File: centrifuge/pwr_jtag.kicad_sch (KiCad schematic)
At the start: 6 parts

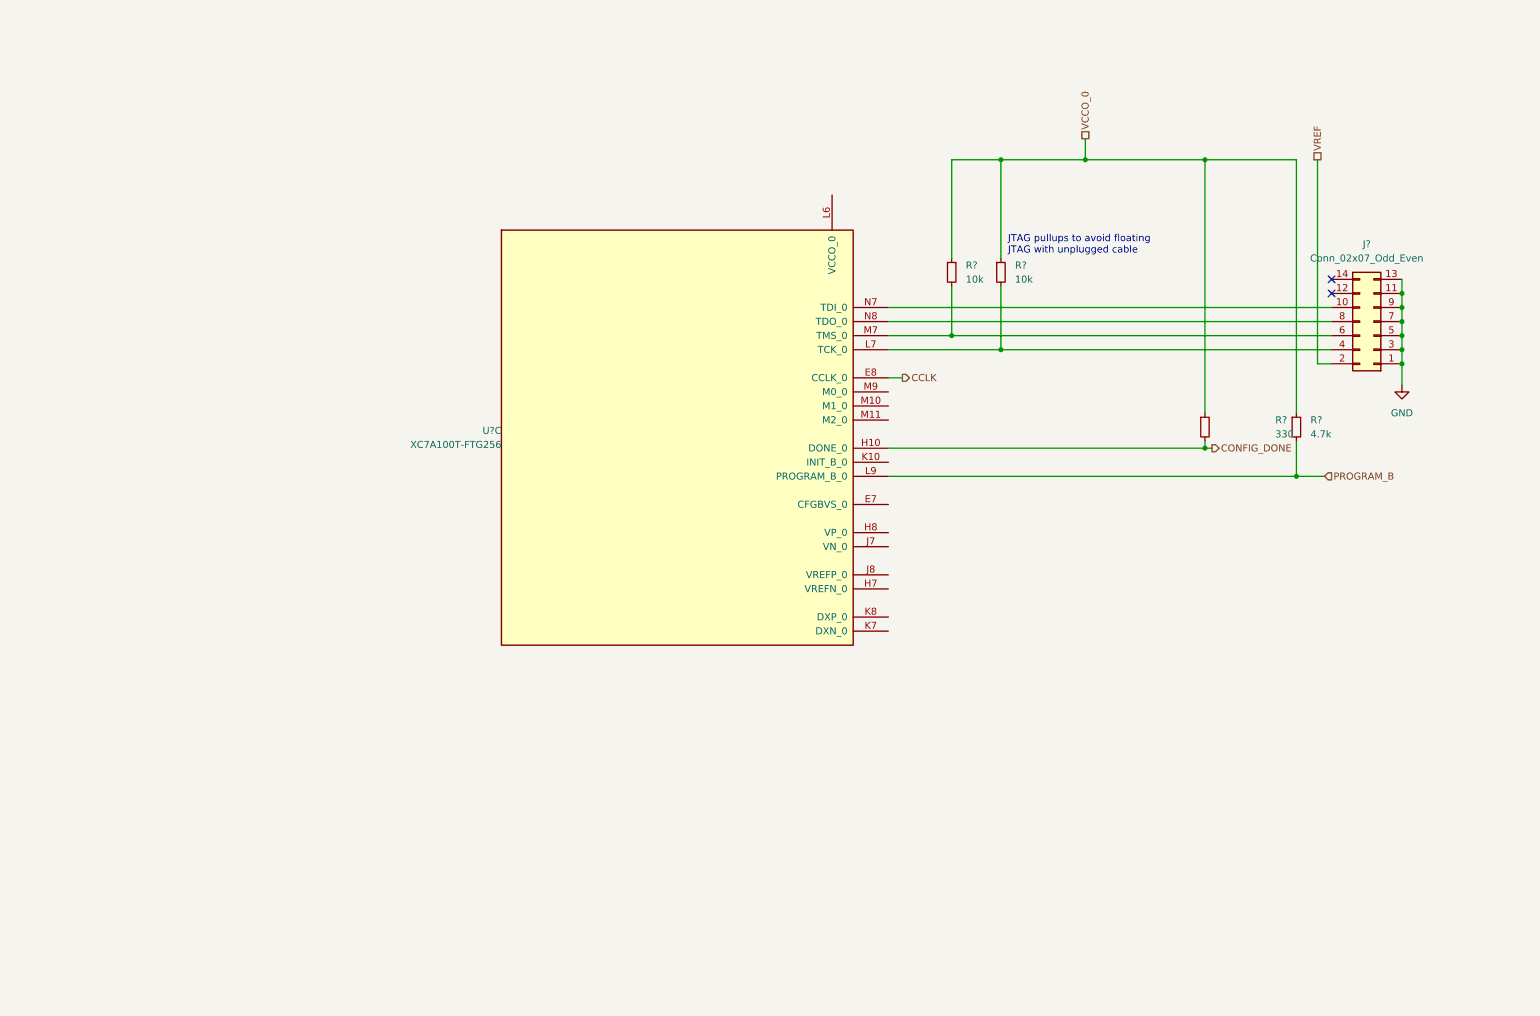
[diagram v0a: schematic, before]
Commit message: Made initial pin map of SRAM-FPGA and possible routing
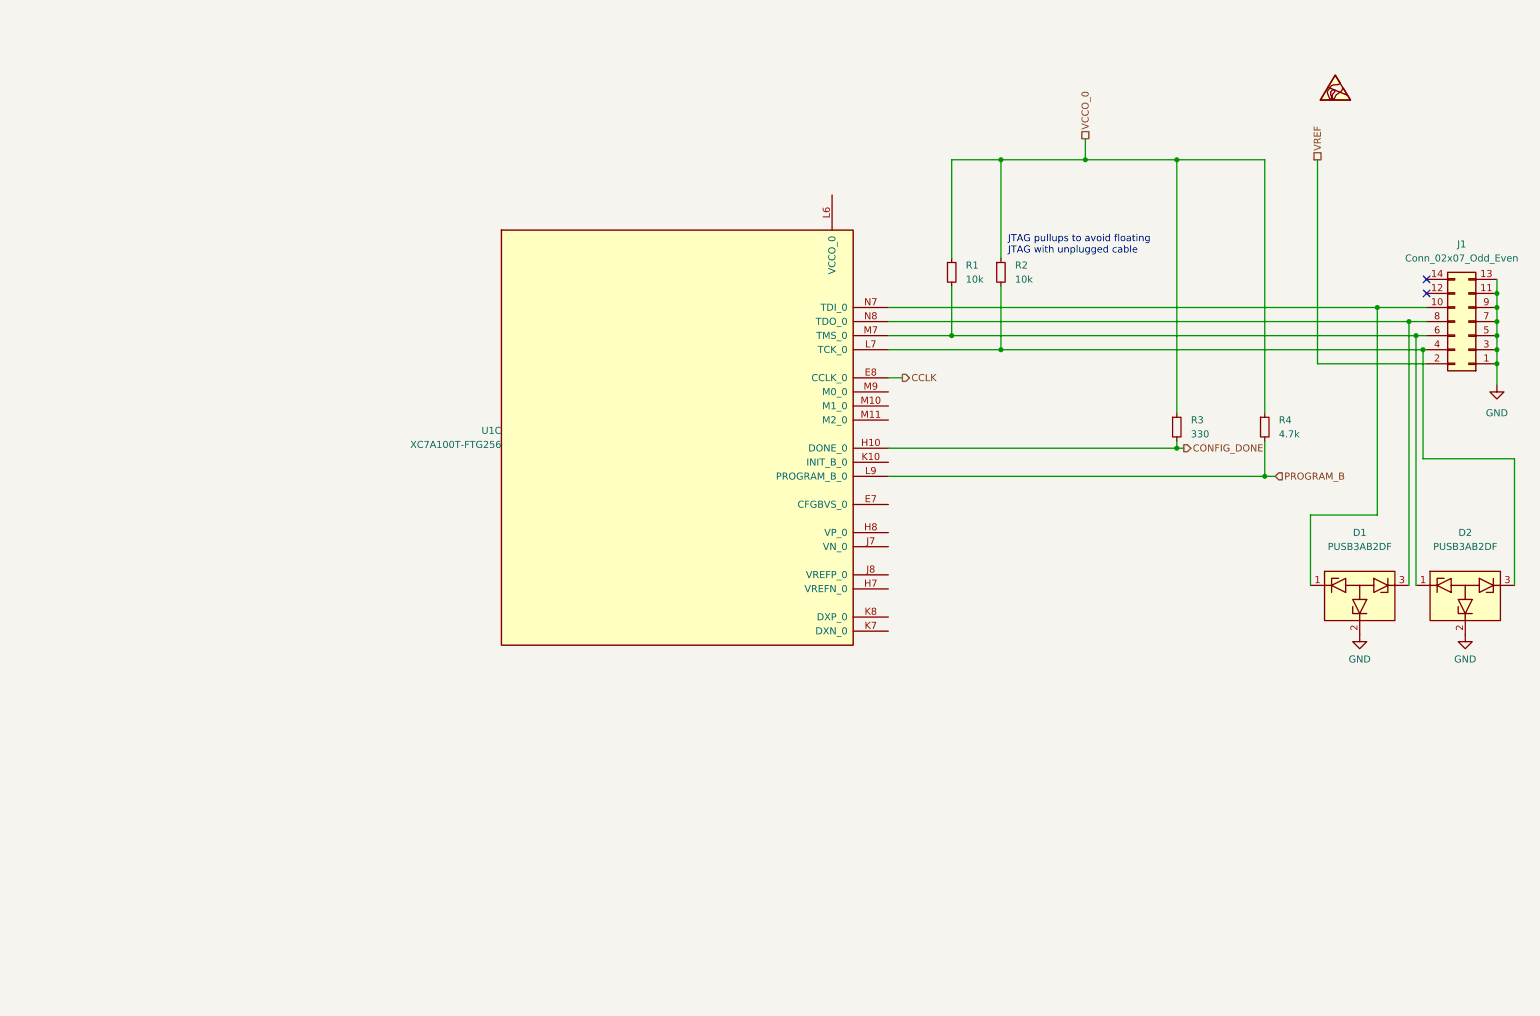
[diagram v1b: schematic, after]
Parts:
- added D1, D2: PUSB3AB2DF, symbol centrifuge_symbols:PUSB3AB2DF
- U1: renamed from U?; footprint (none) -> Package_BGA:Xilinx_FTG256
- gave numbers to parts that had none: 5
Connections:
- net GND: now also D1.2 (K2), D2.2 (K2)
- net at J1.4 (Pin_4), R2.2, U1.L7 (TCK_0): now also D2.3 (K3)
- net at J1.10 (Pin_10), U1.N7 (TDI_0): now also D1.1 (K1)
- net at J1.6 (Pin_6), R1.2, U1.M7 (TMS_0): now also D2.1 (K1)
- net at J1.8 (Pin_8), U1.N8 (TDO_0): now also D1.3 (K3)
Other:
- moved on the sheet: J1, R3, R4

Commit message: Completed majority of schematic, need to add decoupling but otherwise mostly ready
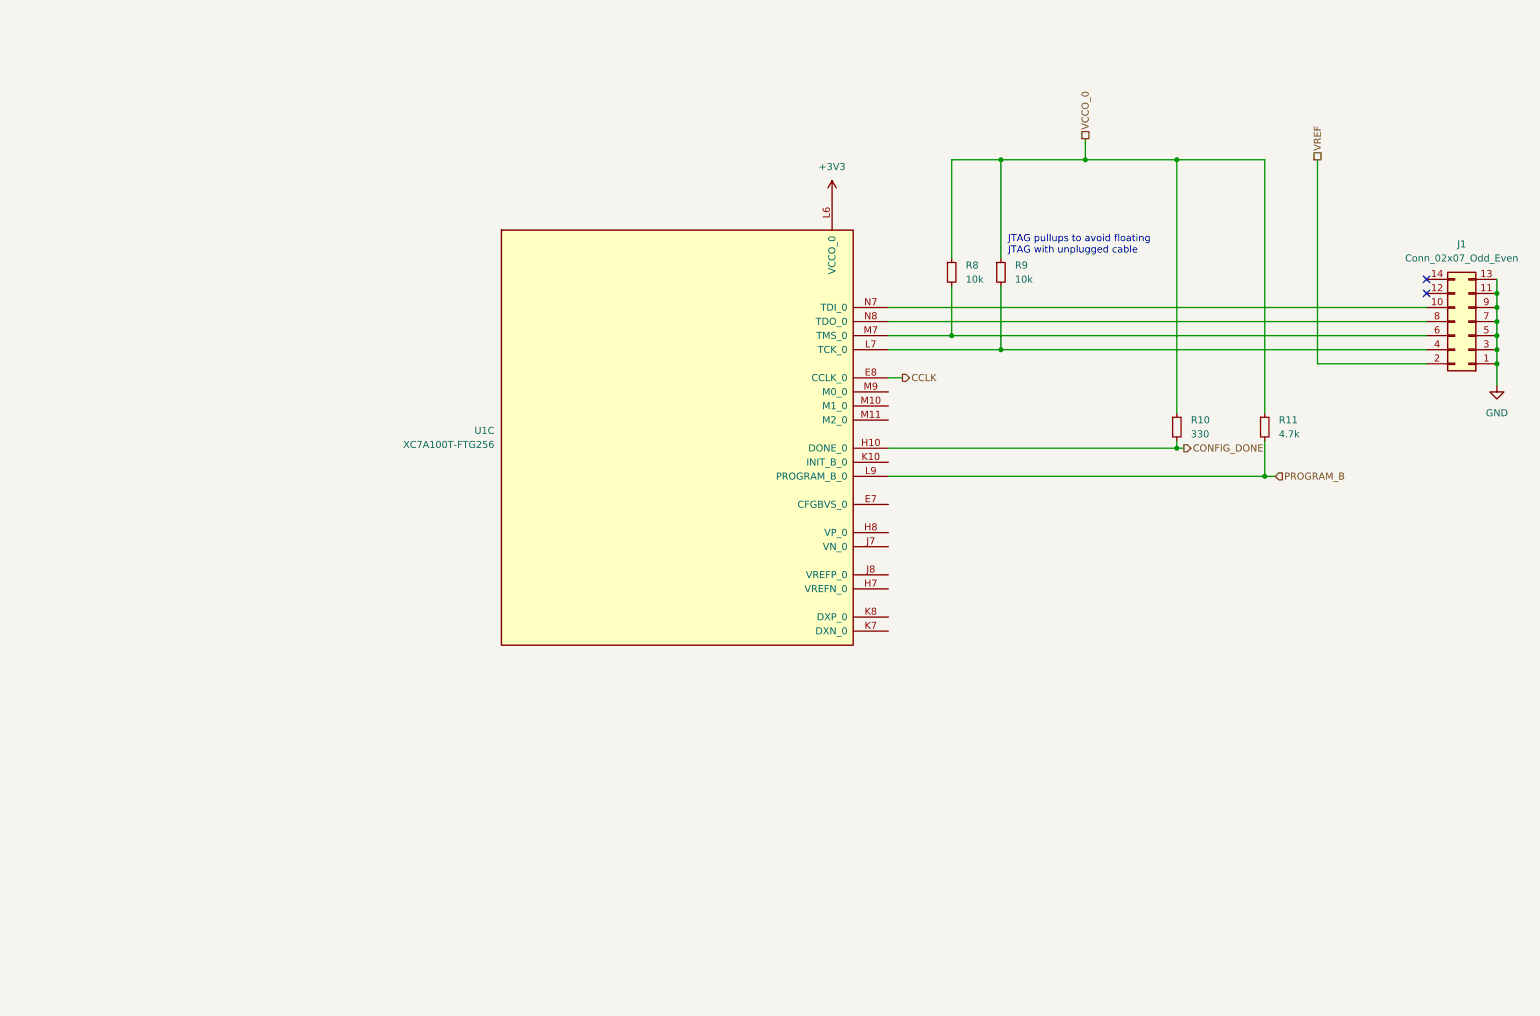
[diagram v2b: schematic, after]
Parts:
- removed D1, D2: PUSB3AB2DF, symbol centrifuge_symbols:PUSB3AB2DF
- J1: footprint (none) -> Connector_IDC:IDC-Header_2x07_P2.54mm_Vertical
- R10: renamed from R3; footprint (none) -> Resistor_SMD:R_0805_2012Metric_Pad1.20x1.40mm_HandSolder; Order Page (none) -> https://no.mouser.com/ProductDetail/Welwyn-Components-TT-El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
- R11: renamed from R4; footprint (none) -> Resistor_SMD:R_0805_2012Metric_Pad1.20x1.40mm_HandSolder; Order Page (none) -> https://no.mouser.com/ProductDetail/YAGEO/RC0805FR-074K7L?q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
- R8: renamed from R1; footprint (none) -> Resistor_SMD:R_0805_2012Metric_Pad1.20x1.40mm_HandSolder; Order Page (none) -> https://no.mouser.com/ProductDetail/YAGEO/RC0805FR-1310KL?q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
- R9: renamed from R2; footprint (none) -> Resistor_SMD:R_0805_2012Metric_Pad1.20x1.40mm_HandSolder; Order Page (none) -> https://no.mouser.com/ProductDetail/YAGEO/RC0805FR-1310KL?q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
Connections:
- net +3V3: now reaches U1.L6 (VCCO_0)
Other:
- title: VGA Centrifuge FPGA board -> VGA Centrifuge

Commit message: FPGA PCB design completed
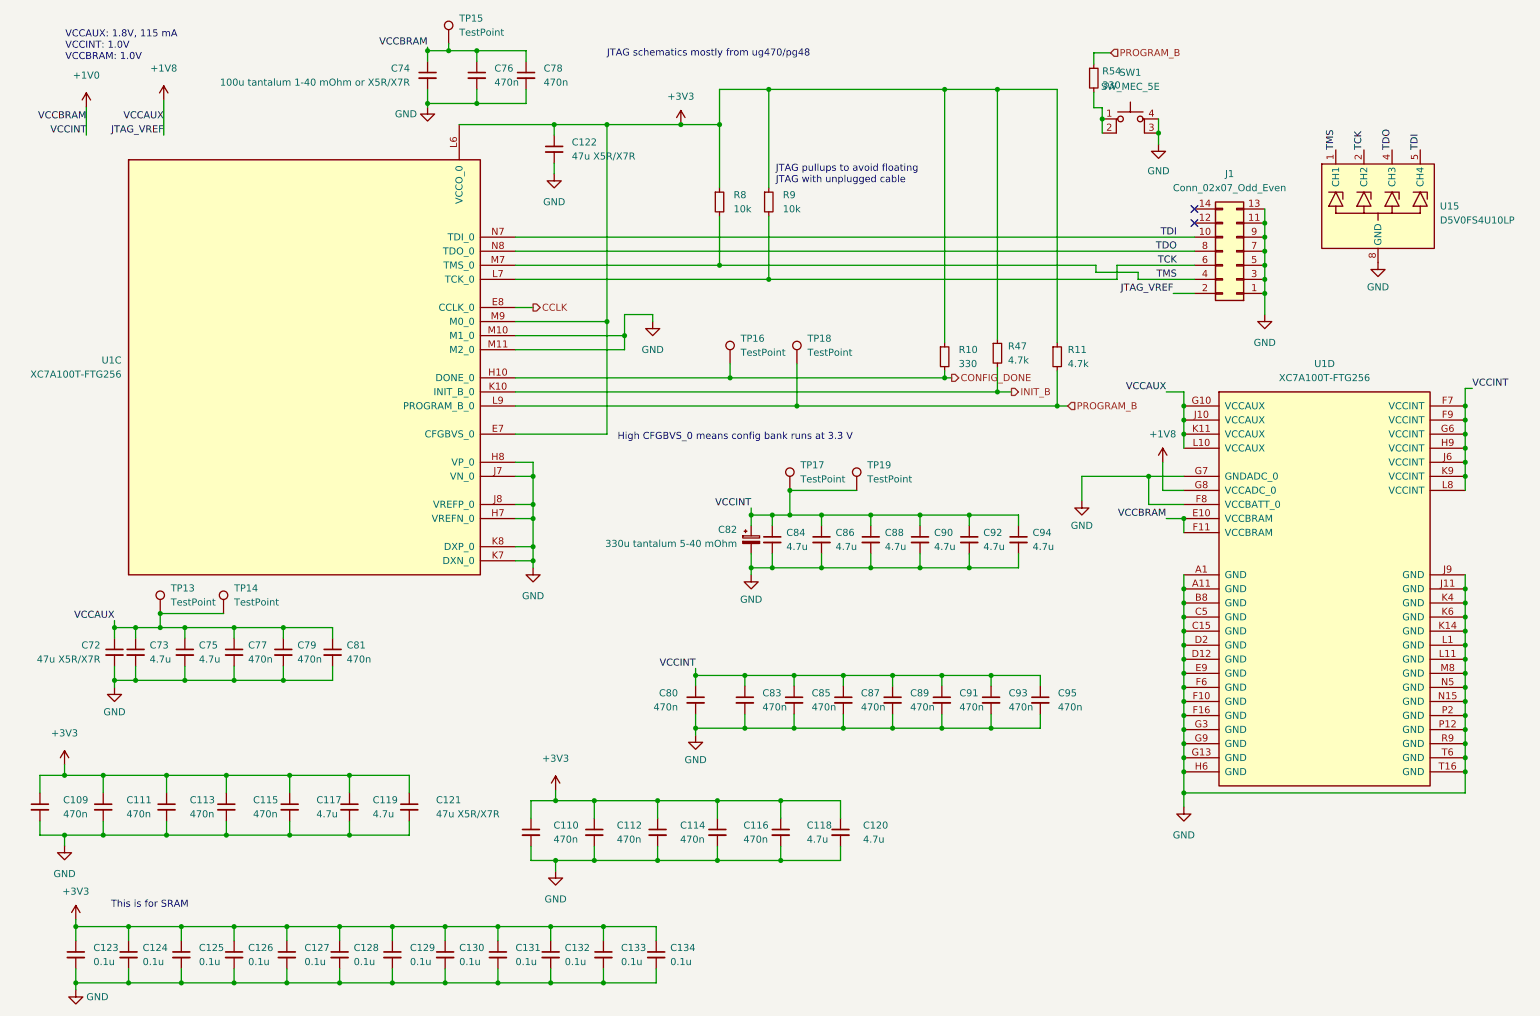
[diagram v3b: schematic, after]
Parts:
- added C109, C110, C111, C112, C113, C114, C115, C116, C76, C77, C78, C79, C80, C81, C83, C85, C87, C89, C91, C93, C95: 470n, Capacitor_SMD:C_0603_1608Metric_Pad1.08x0.95mm_HandSolder, symbol Device:C_Small
- added C117, C118, C119, C120, C73, C75, C84, C86, C88, C90, C92, C94: 4.7u, Capacitor_SMD:C_0805_2012Metric_Pad1.18x1.45mm_HandSolder, symbol Device:C_Small
- added C121, C122, C72: 47u X5R/X7R, Capacitor_SMD:C_1210_3225Metric_Pad1.33x2.70mm_HandSolder, symbol Device:C_Small
- added C123, C124, C125, C126, C127, C128, C129, C130, C131, C132, C133, C134: 0.1u, Capacitor_SMD:C_0805_2012Metric_Pad1.18x1.45mm_HandSolder, symbol Device:C_Small
- added C74: 100u tantalum 1-40 mOhm or X5R/X7R, Capacitor_SMD:C_1210_3225Metric_Pad1.33x2.70mm_HandSolder, symbol Device:C_Small
- added C82: 330u tantalum 5-40 mOhm, Capacitor_Tantalum_SMD:CP_EIA-7343-31_Kemet-D_Pad2.25x2.55mm_HandSolder, symbol Device:C_Polarized_Small
- added R47: 4.7k, Resistor_SMD:R_0805_2012Metric_Pad1.20x1.40mm_HandSolder, symbol Device:R_Small
- added R54: 330, Resistor_SMD:R_0805_2012Metric_Pad1.20x1.40mm_HandSolder, symbol Device:R_Small
- added SW1: SW_MEC_5E, centrifuge footprints:SW_Push_1P1T_NO_6x6mm_H9.5mm_modified, symbol Switch:SW_MEC_5E
- added TP13, TP14, TP15, TP16, TP17, TP18, TP19: TestPoint, TestPoint:TestPoint_Keystone_5015_Micro-Minature, symbol Connector:TestPoint
- added unit 4 of U1
- added U15: D5V0FS4U10LP, Package_DFN_QFN:Diodes_UDFN-10_1.0x2.5mm_P0.5mm, symbol centrifuge_symbols:D5V0FS4U10LP
- J1: footprint Connector_IDC:IDC-Header_2x07_P2.54mm_Vertical -> centrifuge footprints:878311411; Order Page (none) -> https://www.digikey.no/en/products/detail/molex/0878311411/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
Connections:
- net VCCO_0 is gone; now on net +3V3: R10.1, R11.1, R8.1, R9.1
- net +3V3: now also U1.E7 (CFGBVS_0), U1.M9 (M0_0), C109.1, C110.1, C111.1, C112.1, C113.1, C114.1, C115.1, C116.1, C117.1, C118.1, C119.1, C120.1, C121.1, C122.1, C123.1, C124.1, C125.1, C126.1, C127.1, C128.1, C129.1, C130.1, C131.1, C132.1, C133.1, C134.1, R47.1
- net CONFIG_DONE: now also TP16.1
- net GND: now also U1.H7 (VREFN_0), U1.H8 (VP_0), U1.J7 (VN_0), U1.J8 (VREFP_0), U1.K7 (DXN_0), U1.K8 (DXP_0), U1.M10 (M1_0), U1.M11 (M2_0), C109.2, C110.2, C111.2, C112.2, C113.2, C114.2, C115.2, C116.2, C117.2, C118.2, C119.2, C120.2, C121.2, C122.2, C123.2, C124.2, C125.2, C126.2, C127.2, C128.2, C129.2, C130.2, C131.2, C132.2, C133.2, C134.2, C72.2, C73.2, C74.2, C75.2, C76.2, C77.2, C78.2, C79.2, C80.2, C81.2, C82.2, C83.2, C84.2, C85.2, C86.2, C87.2, C88.2, C89.2, C90.2, C91.2, C92.2, C93.2, C94.2, C95.2, SW1.3 (K), SW1.4 (A), U1.A1 (GND), U1.A11 (GND), U1.B8 (GND), U1.C15 (GND), U1.C5 (GND), U1.D12 (GND), U1.D2 (GND), U1.E9 (GND), U1.F10 (GND), U1.F16 (GND), U1.F6 (GND), U1.F8 (VCCBATT_0), U1.G13 (GND), U1.G3 (GND), U1.G7 (GNDADC_0), U1.G9 (GND), U1.H6 (GND), U1.J11 (GND), U1.J9 (GND), U1.K14 (GND), U1.K4 (GND), U1.K6 (GND), U1.L1 (GND), U1.L11 (GND), U1.M8 (GND), U1.N15 (GND), U1.N5 (GND), U1.P12 (GND), U1.P2 (GND), U1.R9 (GND), U1.T16 (GND), U1.T6 (GND), U15.3 (GND), U15.8 (GND)
- net PROGRAM_B: now also R54.1, TP18.1
- net TCK: now reaches R9.2, U1.L7 (TCK_0)
- net TCK: now also J1.6 (Pin_6), U15.2 (CH2); no longer J1.4 (Pin_4)
- net TDI: now reaches J1.10 (Pin_10), U1.N7 (TDI_0)
- net TDI: now also U15.5 (CH4)
- net TMS: now reaches R8.2, U1.M7 (TMS_0)
- net TMS: now also J1.4 (Pin_4), U15.1 (CH1); no longer J1.6 (Pin_6)
- net TDO: now reaches J1.8 (Pin_8), U1.N8 (TDO_0)
- net TDO: now also U15.4 (CH3)
- net INIT_B: now reaches U1.K10 (INIT_B_0)
- net INIT_B: now also R47.2
- net VREF renamed +1V8
- net +1V8: now also C72.1, C73.1, C75.1, C77.1, C79.1, C81.1, TP13.1, TP14.1, U1.G10 (VCCAUX), U1.G8 (VCCADC_0), U1.J10 (VCCAUX), U1.K11 (VCCAUX), U1.L10 (VCCAUX)
- new net: R54.2, SW1.1, SW1.2
- new net +1V0: C74.1, C76.1, C78.1, C80.1, C82.1, C83.1, C84.1, C85.1, C86.1, C87.1, C88.1, C89.1, C90.1, C91.1, C92.1, C93.1, C94.1, C95.1, TP15.1, TP17.1, TP19.1, U1.E10 (VCCBRAM), U1.F11 (VCCBRAM), U1.F7 (VCCINT), U1.F9 (VCCINT), U1.G6 (VCCINT), U1.H9 (VCCINT), U1.J6 (VCCINT), U1.K9 (VCCINT), U1.L8 (VCCINT)
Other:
- note added: "High CFGBVS_0 means config bank runs at 3.3 V"
- note added: "JTAG schematics mostly from ug470/pg48"
- note added: "This is for SRAM"
- note added: "VCCAUX: 1.8V, 115 mA VCCINT: 1.0V VCCBRAM: 1.0V"
- moved on the sheet: J1, R10, R11, R8, R9, U1C
